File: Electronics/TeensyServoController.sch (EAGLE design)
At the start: 96 parts, among them U1 TEENSY_3.1_ALLPINS, U12 MIC5225, U13 MIC5225, U2 AP3211KTR-G1, U3 AP3211KTR-G1, U4 AP3211KTR-G1, U5 AP2210N-3.3TRG1

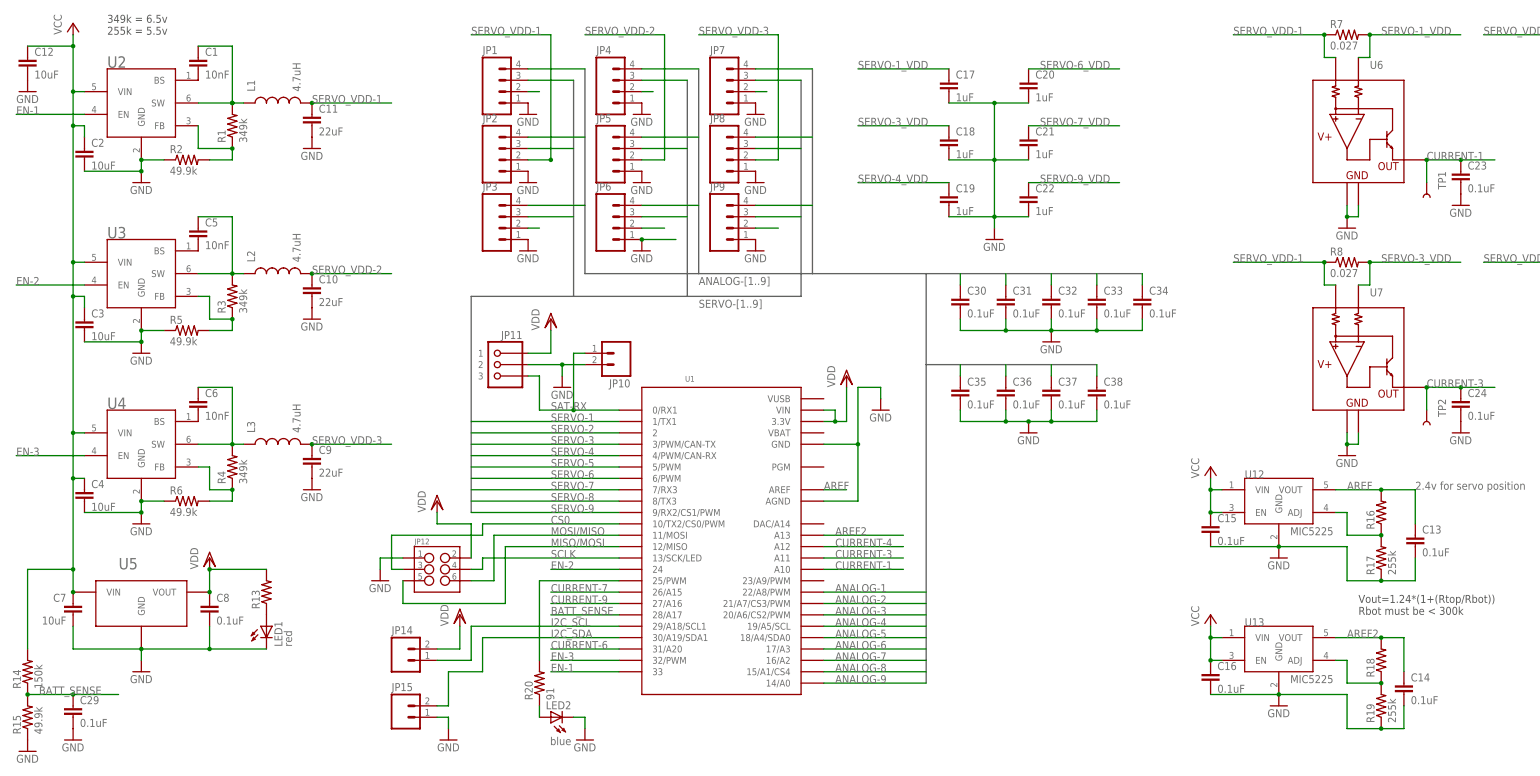
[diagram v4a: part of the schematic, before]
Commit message: Updated PCB design after receiving rev 1
Fixed regulator footprint
Changed a few part packages
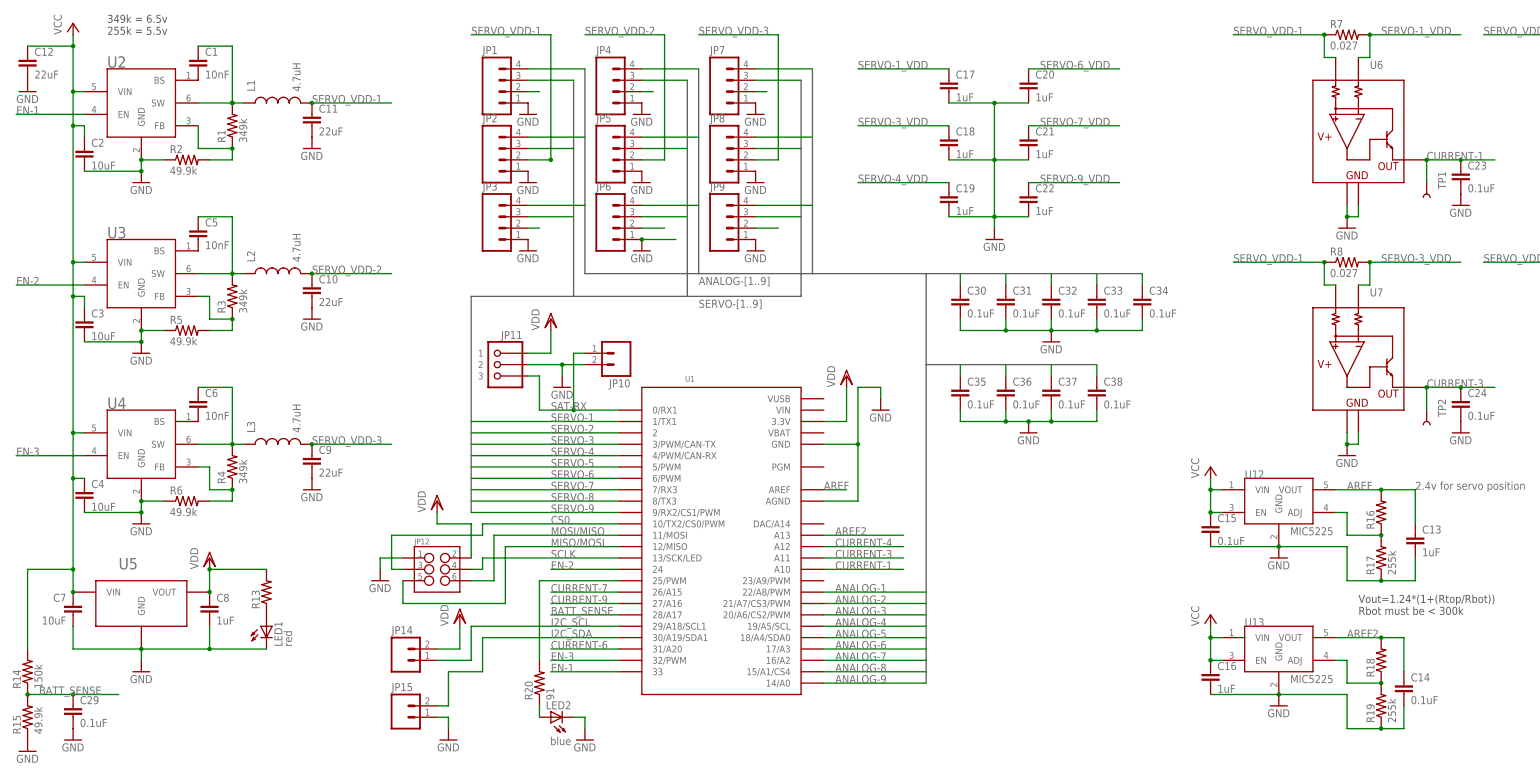
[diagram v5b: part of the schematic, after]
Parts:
- C12: value 10uF -> 22uF
- C13: value 0.1uF -> 1uF; device resistor:C-EUC0402 -> resistor:C-EUC0603
- C16, C8: value 0.1uF -> 1uF
- R16, R17, R18, R19: device resistor:R-US_R0603 -> resistor:R-US_R0402
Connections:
- net VDD: no longer U1.VIN
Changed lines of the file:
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@@
 <grid distance="0.1" unitdist="inch" unit="inch" style="lines" multiple="1" display="no" altdistance="0.01" altunitdist="inch" altunit="inch"/>
 <layers>
-<layer number="1" name="Top" color="4" fill="1" visible="no" active="no"/>
-<layer number="2" name="Route2" color="5" fill="1" visible="no" active="no"/>
-<layer number="3" name="Route3" color="4" fill="1" visible="no" active="no"/>
-<layer number="14" name="Route14" color="1" fill="6" visible="no" active="no"/>
-<layer number="15" name="Route15" color="3" fill="1" visible="no" active="no"/>
-<layer number="16" name="Bottom" color="1" fill="1" visible="no" active="no"/>
-<layer number="17" name="Pads" color="2" fill="1" visible="no" active="no"/>
-<layer number="18" name="Vias" color="2" fill="1" visible="no" active="no"/>
-<layer number="19" name="Unrouted" color="6" fill="1" visible="no" active="no"/>
-<layer number="20" name="Dimension" color="15" fill="1" visible="no" active="no"/>
-<layer number="21" name="tPlace" color="7" fill="1" visible="no" active="no"/>
-<layer number="22" name="bPlace" color="7" fill="1" visible="no" active="no"/>
-<layer number="23" name="tOrigins" color="15" fill="1" visible="no" active="no"/>
-<layer number="24" name="bOrigins" color="15" fill="1" visible="no" active="no"/>
-<layer number="25" name="tNames" color="7" fill="1" visible="no" active="no"/>
-<layer number="26" name="bNames" color="7" fill="1" visible="no" active="no"/>
-<layer number="27" name="tValues" color="7" fill="1" visible="no" active="no"/>
-<layer number="28" name="bValues" color="7" fill="1" visible="no" active="no"/>
+<layer number="1" name="Top" color="4" fill="1" visible="yes" active="no"/>
+<layer number="2" name="Route2" color="5" fill="1" visible="yes" active="no"/>
+<layer number="3" name="Route3" color="4" fill="1" visible="yes" active="no"/>
+<layer number="14" name="Route14" color="1" fill="6" visible="yes" active="no"/>
+<layer number="15" name="Route15" color="3" fill="1" visible="yes" active="no"/>
+<layer number="16" name="Bottom" color="1" fill="1" visible="yes" active="no"/>
+<layer number="17" name="Pads" color="2" fill="1" visible="yes" active="no"/>
+<layer number="18" name="Vias" color="2" fill="1" visible="yes" active="no"/>
+<layer number="19" name="Unrouted" color="6" fill="1" visible="yes" active="no"/>
+<layer number="20" name="Dimension" color="15" fill="1" visible="yes" active="no"/>
+<layer number="21" name="tPlace" color="7" fill="1" visible="yes" active="no"/>
+<layer number="22" name="bPlace" color="7" fill="1" visible="yes" active="no"/>
+<layer number="23" name="tOrigins" color="15" fill="1" visible="yes" active="no"/>
+<layer number="24" name="bOrigins" color="15" fill="1" visible="yes" active="no"/>
+<layer number="25" name="tNames" color="7" fill="1" visible="yes" active="no"/>
+<layer number="26" name="bNames" color="7" fill="1" visible="yes" active="no"/>
+<layer number="27" name="tValues" color="7" fill="1" visible="yes" active="no"/>
+<layer number="28" name="bValues" color="7" fill="1" visible="yes" active="no"/>
 <layer number="29" name="tStop" color="7" fill="3" visible="no" active="no"/>
 <layer number="30" name="bStop" color="7" fill="6" visible="no" active="no"/>
@@
 <layer number="35" name="tGlue" color="7" fill="4" visible="no" active="no"/>
 <layer number="36" name="bGlue" color="7" fill="5" visible="no" active="no"/>
-<layer number="37" name="tTest" color="7" fill="1" visible="no" active="no"/>
-<layer number="38" name="bTest" color="7" fill="1" visible="no" active="no"/>
+<layer number="37" name="tTest" color="7" fill="1" visible="yes" active="no"/>
+<layer number="38" name="bTest" color="7" fill="1" visible="yes" active="no"/>
 <layer number="39" name="tKeepout" color="4" fill="11" visible="no" active="no"/>
 <layer number="40" name="bKeepout" color="1" fill="11" visible="no" active="no"/>
@@
 <layer number="44" name="Drills" color="7" fill="1" visible="no" active="no"/>
 <layer number="45" name="Holes" color="7" fill="1" visible="no" active="no"/>
-<layer number="46" name="Milling" color="3" fill="1" visible="no" active="no"/>
-<layer number="47" name="Measures" color="7" fill="1" visible="no" active="no"/>
-<layer number="48" name="Document" color="7" fill="1" visible="no" active="no"/>
-<layer number="49" name="Reference" color="7" fill="1" visible="no" active="no"/>
-<layer number="50" name="dxf" color="7" fill="1" visible="no" active="no"/>
-<layer number="51" name="tDocu" color="7" fill="1" visible="no" active="no"/>
-<layer number="52" name="bDocu" color="7" fill="1" visible="no" active="no"/>
-<layer number="53" name="tGND_GNDA" color="7" fill="9" visible="no" active="no"/>
-<layer number="54" name="bGND_GNDA" color="1" fill="9" visible="no" active="no"/>
-<layer number="56" name="wert" color="7" fill="1" visible="no" active="no"/>
+<layer number="46" name="Milling" color="3" fill="1" visible="yes" active="no"/>
+<layer number="47" name="Measures" color="7" fill="1" visible="yes" active="no"/>
+<layer number="48" name="Document" color="7" fill="1" visible="yes" active="no"/>
+<layer number="49" name="Reference" color="7" fill="1" visible="yes" active="no"/>
+<layer number="50" name="dxf" color="7" fill="1" visible="yes" active="no"/>
+<layer number="51" name="tDocu" color="7" fill="1" visible="yes" active="no"/>
+<layer number="52" name="bDocu" color="7" fill="1" visible="yes" active="no"/>
+<layer number="53" name="tGND_GNDA" color="7" fill="9" visible="yes" active="no"/>
+<layer number="54" name="bGND_GNDA" color="1" fill="9" visible="yes" active="no"/>
+<layer number="56" name="wert" color="7" fill="1" visible="yes" active="no"/>
 <layer number="90" name="Modules" color="5" fill="1" visible="yes" active="yes"/>
 <layer number="91" name="Nets" color="2" fill="1" visible="yes" active="yes"/>
@@
 <part name="VDD5" library="supply1" deviceset="VDD" device=""/>
 <part name="C7" library="resistor" deviceset="C-EU" device="C0805" value="10uF"/>
-<part name="C8" library="resistor" deviceset="C-EU" device="C0603" value="0.1uF"/>
+<part name="C8" library="resistor" deviceset="C-EU" device="C0603" value="1uF"/>
 <part name="GND16" library="supply1" deviceset="GND" device=""/>
 <part name="JP11" library="My Parts" deviceset="3-PIN_JST_ZH_PTH_CONNECTOR" device="RIGHT_ANGLE_PTH"/>
@@
 <part name="GND25" library="supply1" deviceset="GND" device=""/>
 <part name="GND26" library="supply1" deviceset="GND" device=""/>
-<part name="C12" library="resistor" deviceset="C-EU" device="C0805" value="10uF"/>
+<part name="C12" library="resistor" deviceset="C-EU" device="C0805" value="22uF"/>
 <part name="GND27" library="supply1" deviceset="GND" device=""/>
 <part name="TP2" library="SparkFun-Passives" deviceset="TEST-POINT" device="3" value=""/>
@@
 <part name="P+2" library="supply1" deviceset="VCC" device=""/>
 <part name="GND29" library="supply1" deviceset="GND" device=""/>
-<part name="R16" library="resistor" deviceset="R-US_" device="R0603"/>
-<part name="R17" library="resistor" deviceset="R-US_" device="R0603" value="255k"/>
+<part name="R16" library="resistor" deviceset="R-US_" device="R0402"/>
+<part name="R17" library="resistor" deviceset="R-US_" device="R0402" value="255k"/>
 <part name="U13" library="My Parts" deviceset="MIC5225" device=""/>
 <part name="P+3" library="supply1" deviceset="VCC" device=""/>
 <part name="GND30" library="supply1" deviceset="GND" device=""/>
-<part name="R18" library="resistor" deviceset="R-US_" device="R0603"/>
-<part name="R19" library="resistor" deviceset="R-US_" device="R0603" value="255k"/>
+<part name="R18" library="resistor" deviceset="R-US_" device="R0402"/>
+<part name="R19" library="resistor" deviceset="R-US_" device="R0402" value="255k"/>
 <part name="JP14" library="SparkFun-Connectors" deviceset="M02" device="PTH"/>
 <part name="JP15" library="SparkFun-Connectors" deviceset="M02" device="PTH"/>
-<part name="C13" library="resistor" deviceset="C-EU" device="C0402" value="0.1uF"/>
+<part name="C13" library="resistor" deviceset="C-EU" device="C0603" value="1uF"/>
 <part name="C14" library="resistor" deviceset="C-EU" device="C0402" value="0.1uF"/>
 <part name="C15" library="resistor" deviceset="C-EU" device="C0603" value="0.1uF"/>
-<part name="C16" library="resistor" deviceset="C-EU" device="C0603" value="0.1uF"/>
+<part name="C16" library="resistor" deviceset="C-EU" device="C0603" value="1uF"/>
 <part name="LED2" library="SparkFun-LED" deviceset="LED" device="0603" value="blue"/>
 <part name="R20" library="resistor" deviceset="R-US_" device="R0402" value="91"/>
@@
 <pinref part="U1" gate="G$1" pin="3.3V"/>
 <pinref part="VDD4" gate="G$1" pin="VDD"/>
-<wire x1="182.88" y1="27.94" x2="185.42" y2="27.94" width="0.1524" layer="91"/>
-<wire x1="185.42" y1="27.94" x2="187.96" y2="27.94" width="0.1524" layer="91"/>
+<wire x1="182.88" y1="27.94" x2="187.96" y2="27.94" width="0.1524" layer="91"/>
 <wire x1="187.96" y1="27.94" x2="187.96" y2="35.56" width="0.1524" layer="91"/>
-<pinref part="U1" gate="G$1" pin="VIN"/>
-<wire x1="182.88" y1="30.48" x2="185.42" y2="30.48" width="0.1524" layer="91"/>
-<wire x1="185.42" y1="30.48" x2="185.42" y2="27.94" width="0.1524" layer="91"/>
-<junction x="185.42" y="27.94"/>
-</segment>
-<segment>
+</segment>
+<segment>
